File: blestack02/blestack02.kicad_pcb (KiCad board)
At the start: 4 copper layers, 30 x 31.6 mm, 24 parts, among them J1 UART, J2 VIN, SW1 RST, SW2 BOOT, U1 AMS1117-3.3, U2 ESP32-WROOM-32

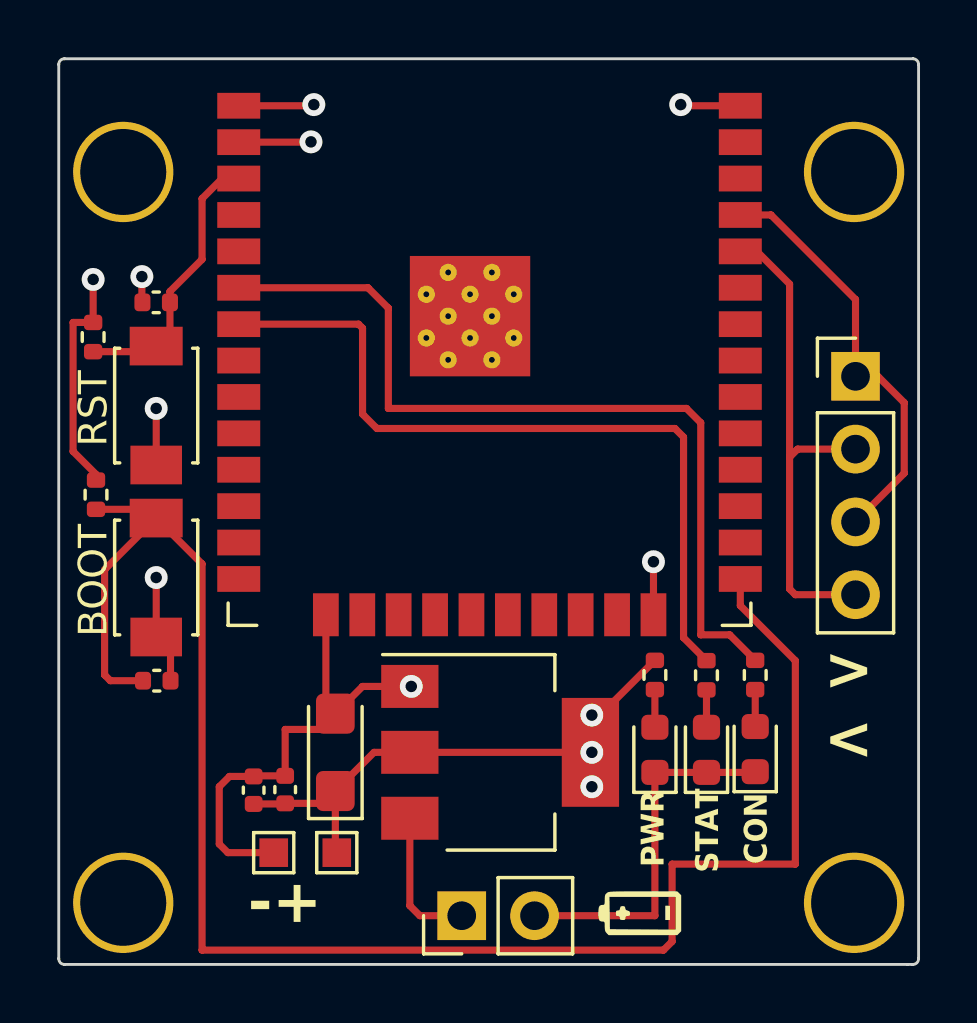
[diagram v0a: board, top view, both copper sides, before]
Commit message: [blestack02] Update pins for stat and con leds
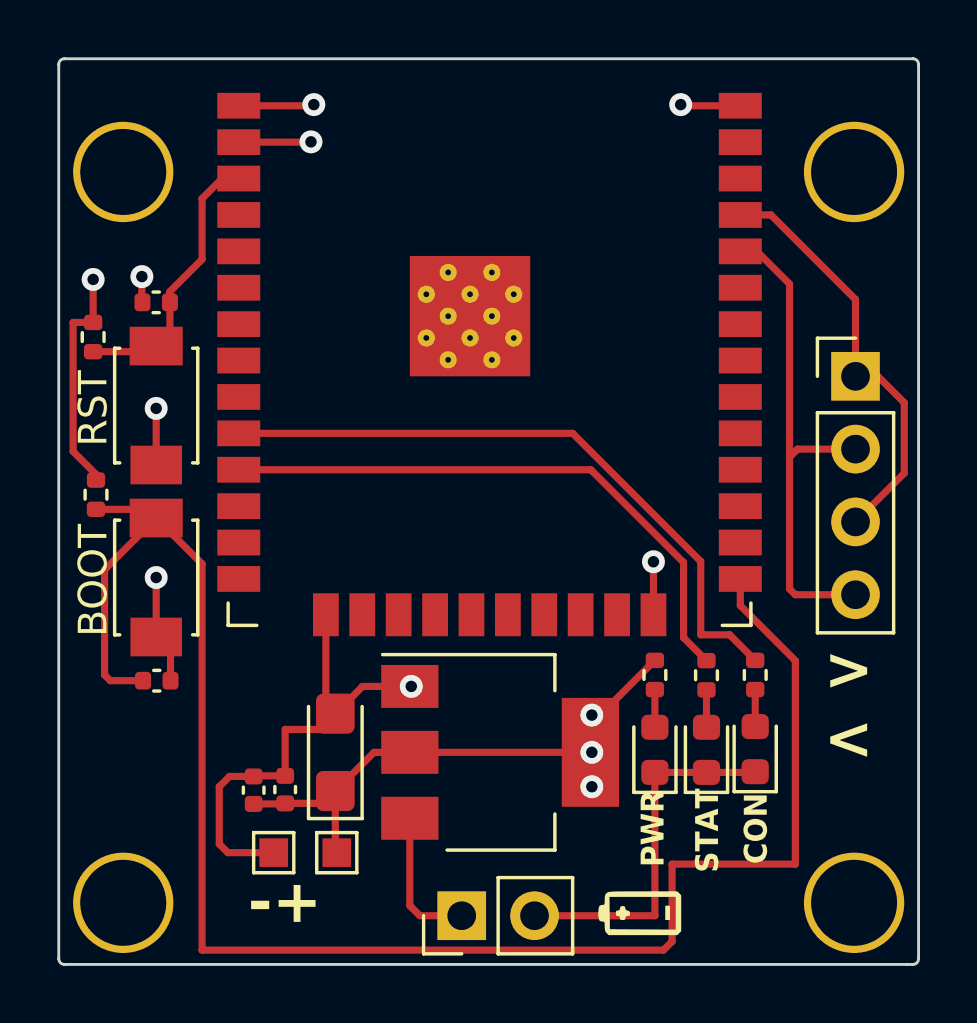
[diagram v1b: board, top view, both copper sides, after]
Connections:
- R4 pad 1: Net-(U2-IO35) -> Net-(U2-IO26)
- R5 pad 1: Net-(U2-IO34) -> Net-(U2-IO25)
- U2 pad 10: unconnected-(U2-IO25-Pad10) -> Net-(U2-IO25)
- U2 pad 11: unconnected-(U2-IO26-Pad11) -> Net-(U2-IO26)
- U2 pad 6: Net-(U2-IO34) -> unconnected-(U2-IO34-Pad6)
- U2 pad 7: Net-(U2-IO35) -> unconnected-(U2-IO35-Pad7)
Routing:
- net Net-(U2-IO34): track 29.8 -> 0.00 mm
- net Net-(U2-IO35): track 27.0 -> 0.00 mm
- net Net-(U2-IO25): track 0.00 -> 22.8 mm
- net Net-(U2-IO26): track 0.00 -> 20.6 mm
